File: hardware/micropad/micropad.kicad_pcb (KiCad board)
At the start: 2 copper layers, 24 parts, among them J1 OLED Connector, J2 Conn_ARM_JTAG_SWD_10, J3 USB_B_Micro, SW1 SW_SPST, SW2 SW_SPST, SW3 SW_SPST, U1 LD1117S33TR_SOT223, U2 STM32F042K6Ux

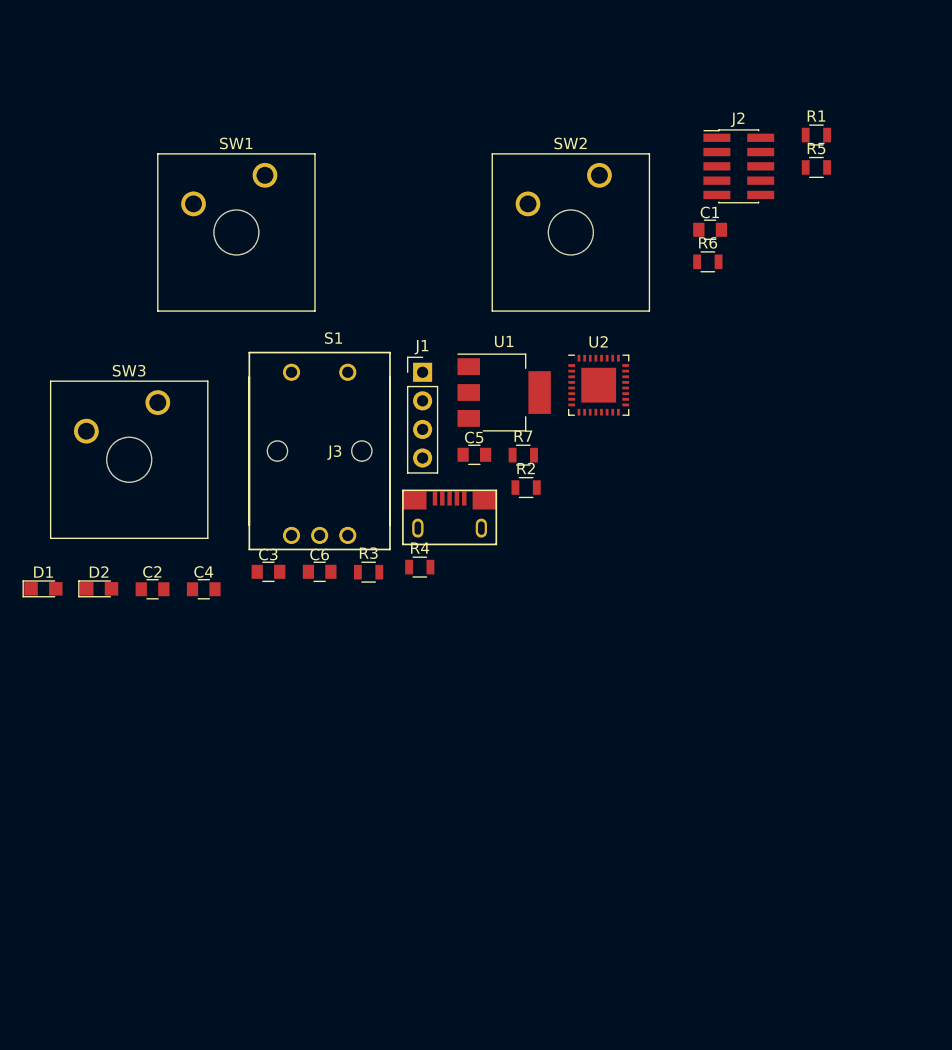
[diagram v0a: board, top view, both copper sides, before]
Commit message: Swap in an APA102 instead of the OLED screen
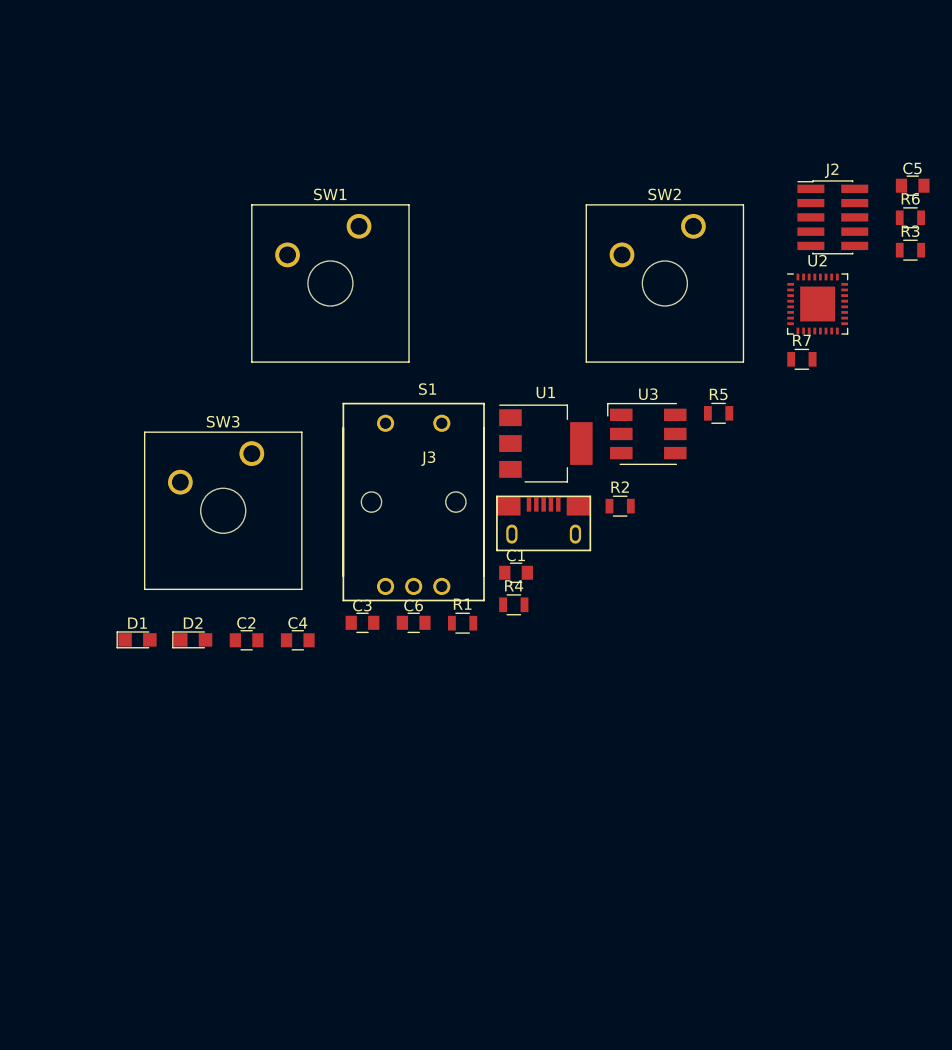
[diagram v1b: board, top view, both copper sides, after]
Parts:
- removed J1: OLED Connector, Pin_Headers:Pin_Header_Straight_1x04_Pitch2.54mm
- added U3: APA102, LEDs:LED_RGB_5050-6, F.Cu at (73.9, 48.8)
- moved R3 56.0 mm to (97.2, 32.5)
- moved R1 53.6 mm to (57.4, 65.7)
- moved C5 45.7 mm to (97.4, 26.8)
- moved C1 35.0 mm to (62.2, 61.2)
- moved R7 26.2 mm to (87.6, 42.2)
- moved R5 23.5 mm to (80.2, 47.0)
- moved U2 20.8 mm to (89.0, 37.3)
- moved R6 18.4 mm to (97.2, 29.6)
- moved C2 9.51 mm to (38.2, 67.2)
- moved C3 9.51 mm to (48.5, 65.6)
- moved C4 9.51 mm to (42.8, 67.2)
- moved C6 9.51 mm to (53.1, 65.6)
- moved D1 9.51 mm to (28.5, 67.1)
- moved D2 9.51 mm to (33.5, 67.1)
- moved J2 9.51 mm to (90.3, 29.6)
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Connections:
- U2 pad 10: Net-(SW2-Pad1) -> Net-(U2-Pad10)
- U2 pad 11: Net-(SW3-Pad1) -> /APA_SCK
- U2 pad 12: /LED_USR -> Net-(U2-Pad12)
- U2 pad 13: Net-(U2-Pad13) -> /APA_MOSI
- U2 pad 18: Net-(U2-Pad18) -> /ENC_A
- U2 pad 19: Net-(U2-Pad19) -> /ENC_B
- U2 pad 20: Net-(U2-Pad20) -> /LED_USR
- U2 pad 29: /I2C_SCL -> Net-(U2-Pad29)
- U2 pad 30: /I2C_SDA -> Net-(U2-Pad30)
- U2 pad 6: /ENC_A -> /BOOT
- U2 pad 7: /ENC_B -> Net-(SW2-Pad1)
- U2 pad 8: /ENC_BTN -> Net-(SW3-Pad1)
- U2 pad 9: /BOOT -> /ENC_BTN

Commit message: Start placing preliminary components
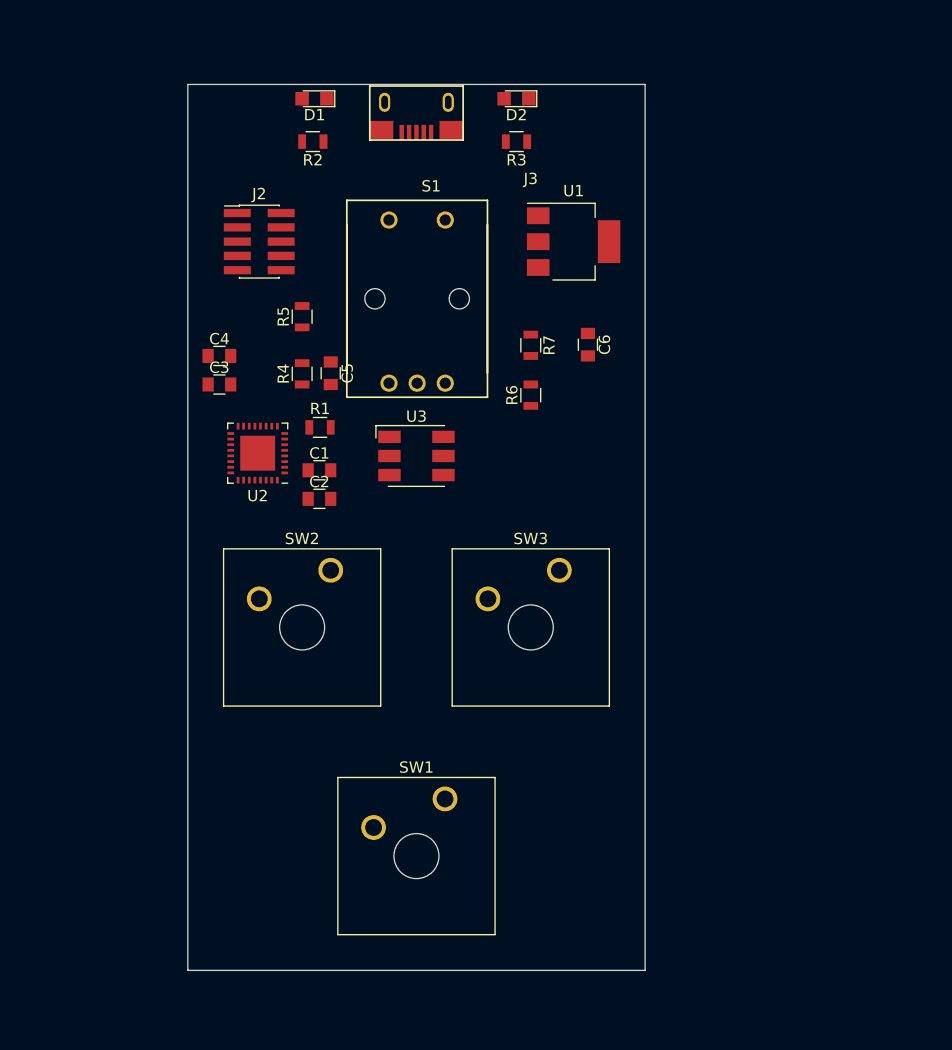
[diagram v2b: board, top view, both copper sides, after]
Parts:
- moved D2 56.0 mm to (62.2, 19.1), turned to 180 degrees
- moved C5 54.3 mm to (45.7, 43.5), turned to 270 degrees
- moved U2 51.5 mm to (39.2, 50.5), turned to 180 degrees
- moved SW1 51.5 mm to (55.9, 81.3)
- moved J2 51.0 mm to (39.4, 31.8)
- moved D1 50.6 mm to (44.3, 19.1), turned to 180 degrees
- moved SW2 44.4 mm to (45.7, 61.0)
- moved R2 42.4 mm to (44.1, 22.9), turned to 180 degrees
- moved J3 38.2 mm to (53.3, 20.3), turned to 180 degrees
- moved R5 38.0 mm to (43.2, 38.4), turned to 90 degrees
- moved R6 37.2 mm to (63.5, 45.4), turned to 90 degrees
- moved R3 36.3 mm to (62.2, 22.9), turned to 180 degrees
- moved SW3 29.2 mm to (66.0, 61.0)
- moved C6 29.2 mm to (68.6, 40.9), turned to 270 degrees
- moved R4 27.8 mm to (43.2, 43.5), turned to 90 degrees
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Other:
- board outline added: 40.6 x 78.7 mm

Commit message: Use a QFN32 package that's easier to work with
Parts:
- U2: footprint Housings_DFN_QFN:WQFN-32-1EP_5x5mm_Pitch0.5mm -> Housings_DFN_QFN:QFN-32-1EP_5x5mm_Pitch0.5mm
- moved U2 1.16 mm to (38.1, 50.8), turned to 0 degrees

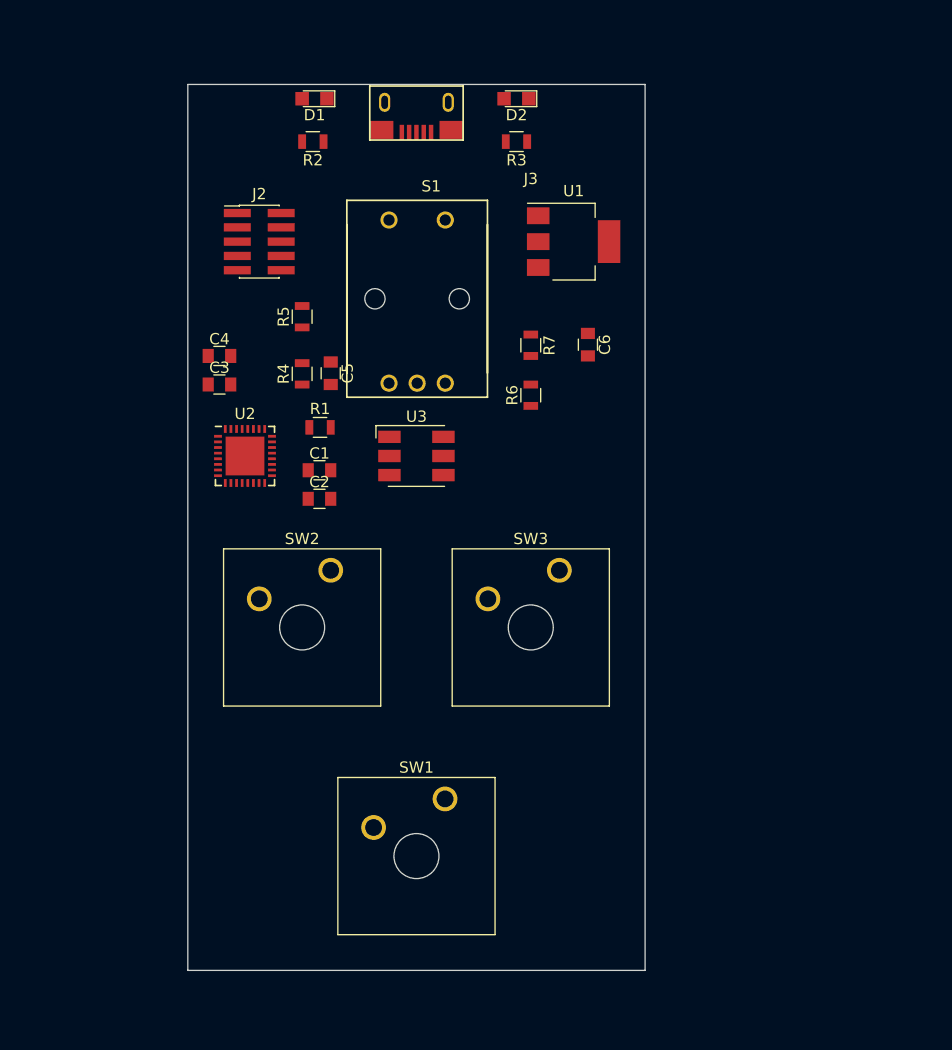
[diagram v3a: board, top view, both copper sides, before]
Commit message: Add mounting holes
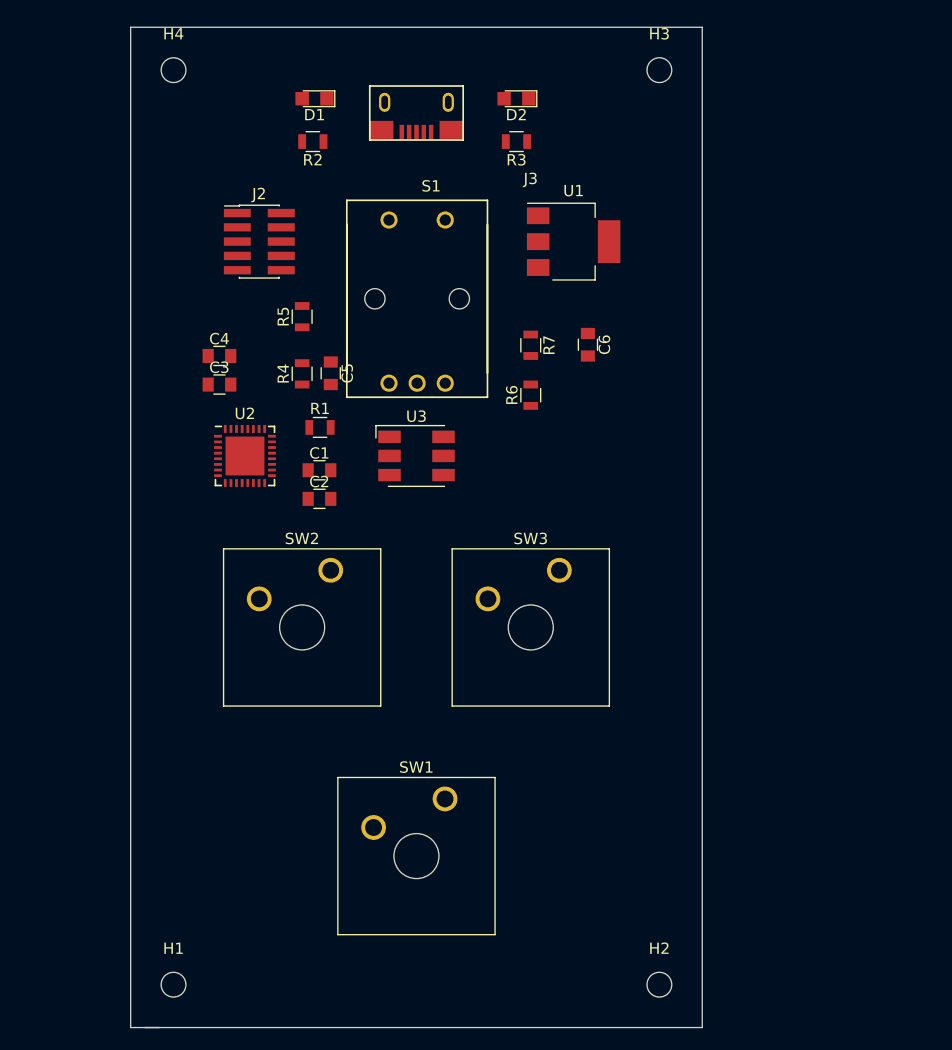
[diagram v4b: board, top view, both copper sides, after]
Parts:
- added H1: MountingHole, Mounting_Holes:MountingHole_2.2mm_M2, F.Cu at (31.8, 97.8)
- added H2: MountingHole, Mounting_Holes:MountingHole_2.2mm_M2, F.Cu at (74.9, 97.8)
- added H3: MountingHole, Mounting_Holes:MountingHole_2.2mm_M2, F.Cu at (74.9, 16.5)
- added H4: MountingHole, Mounting_Holes:MountingHole_2.2mm_M2, F.Cu at (31.8, 16.5)
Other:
- board size 40.6 x 78.7 mm -> 50.8 x 88.9 mm

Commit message: Route remaining tracks
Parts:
- U1: footprint TO_SOT_Packages_SMD:SOT-223-3_TabPin2 -> TO_SOT_Packages_SMD:SOT-223
- moved J3 5.08 mm to (53.3, 15.2)
- moved U1 0.92 mm to (66.5, 31.2)
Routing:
- net +3V3: track 0.00 -> 290.4 mm, vias 0 -> 9
- net /BOOT: track 0.00 -> 57.8 mm, vias 0 -> 2
- net /ENC_BTN: track 0.00 -> 51.2 mm, vias 0 -> 4
- net /LED_USR: track 0.00 -> 48.0 mm, vias 0 -> 4
- net /USB_DM: track 0.00 -> 43.6 mm, vias 0 -> 2
- net /USB_DP: track 0.00 -> 43.0 mm, vias 0 -> 2
- net +5V: track 0.00 -> 42.7 mm
- net Net-(SW3-Pad1): track 0.00 -> 38.9 mm, vias 0 -> 1
- net /ENC_B: track 0.00 -> 38.8 mm, vias 0 -> 2
- net GND: track 0.00 -> 37.3 mm, vias 0 -> 16
- net /SWDIO: track 0.00 -> 25.9 mm
- net /SWCLK: track 0.00 -> 24.2 mm
- net Net-(R4-Pad1): track 0.00 -> 23.9 mm, vias 0 -> 4
- net Net-(SW2-Pad1): track 0.00 -> 23.2 mm, vias 0 -> 1
- net /APA_MOSI: track 0.00 -> 23.1 mm, vias 0 -> 2
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- added copper zone on B.Cu, net GND
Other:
- outline, holes or cut-outs redrawn
- rule trace_min: 0.2 -> 0.127
- rule via_min_drill: 0.3 -> 0.2
- rule via_min_size: 0.4 -> 0.45
